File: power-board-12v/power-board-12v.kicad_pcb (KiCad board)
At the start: 2 copper layers, 22.2 x 17.1 mm, 13 parts, among them J1 Conn_01x01, J2 Conn_01x01, J3 Conn_01x04, U1 L78L12_SOT89, U2 L79L12_SOT89, U3 L78L05_SOT89

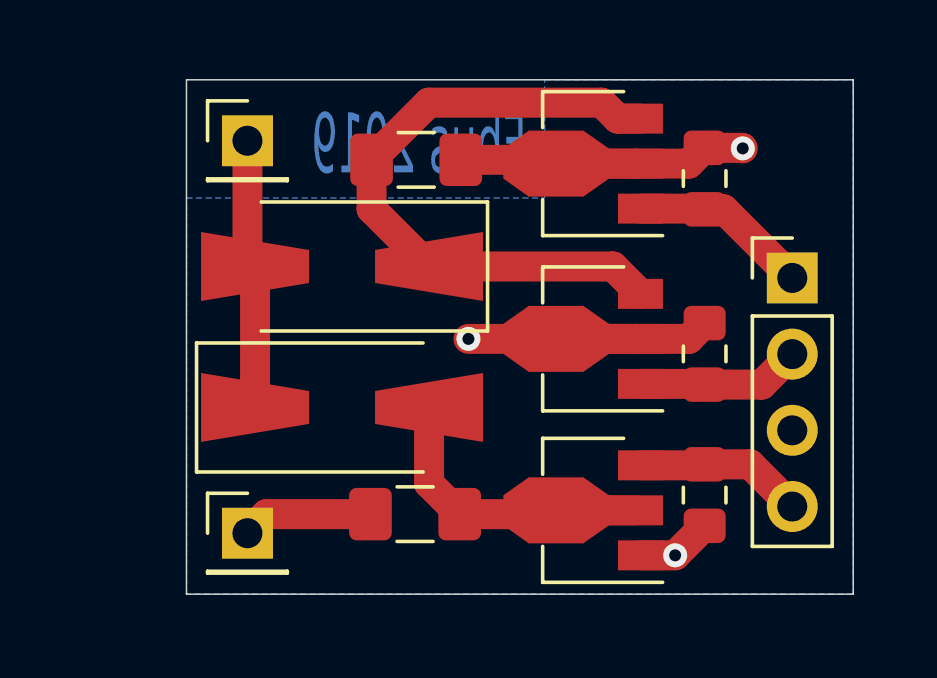
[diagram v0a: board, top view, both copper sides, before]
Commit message: Updated both the amp-and-switch board and the power-board-12v board to version 0.2 after performing bring-up and fixing many issues.
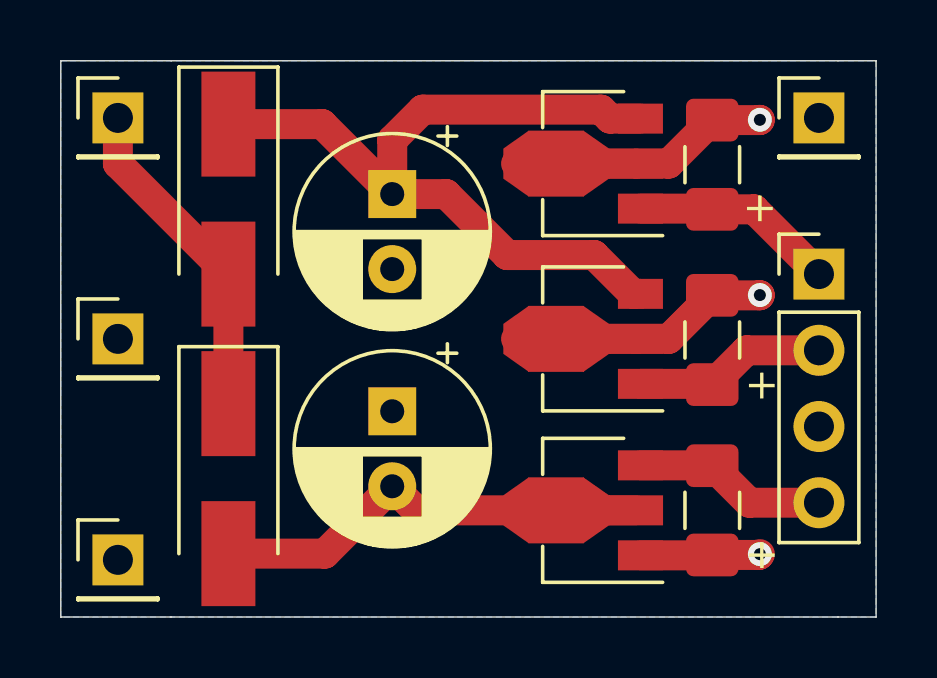
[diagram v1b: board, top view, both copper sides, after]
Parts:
- added J2: Conn_01x01, Connector_PinHeader_2.54mm:PinHeader_1x01_P2.54mm_Vertical, F.Cu at (127.5, 58.2)
- added J2: Conn_01x01, Connector_PinHeader_2.54mm:PinHeader_1x01_P2.54mm_Vertical, F.Cu at (104.1, 72.9)
- C1, C2: value 4.7 uF -> 220 uF; footprint Capacitor_SMD:C_1206_3216Metric_Pad1.42x1.75mm_HandSolder -> Capacitor_THT:CP_Radial_D6.3mm_P2.50mm
- C3, C4, C5: value 0.1 uF -> 4.7 uF; footprint Capacitor_SMD:C_0805_2012Metric_Pad1.15x1.40mm_HandSolder -> Capacitor_SMD:C_1206_3216Metric_Pad1.42x1.75mm_HandSolder
- D1, D2: footprint Diode_SMD:D_SMA-SMB_Universal_Handsoldering -> Diode_SMD:D_SMA_Handsoldering
- moved J2 7.78 mm to (104.1, 65.5)
- moved D2 4.47 mm to (107.8, 70.2), turned to 270 degrees
- moved D1 4.40 mm to (107.8, 60.9), turned to 270 degrees
- moved J1 4.38 mm to (104.1, 58.2)
- moved C2 3.51 mm to (113.3, 67.9), turned to 270 degrees
- moved C1 1.39 mm to (113.3, 60.7), turned to 270 degrees
- moved J3 0.90 mm to (127.5, 63.4)
- moved C4 0.57 mm to (124.0, 71.2)
- moved C3 0.53 mm to (124.0, 65.6)
- moved C5 0.53 mm to (124.0, 59.7)
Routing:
- net Net-(C1-Pad1): track 21.7 -> 26.7 mm
- net Net-(C2-Pad2): track 9.91 -> 14.9 mm
- net GND: track 24.7 -> 21.6 mm
- net Net-(D1-Pad2): track 9.00 -> 11.1 mm
- net Net-(C3-Pad1): track 5.49 -> 6.43 mm
- net Net-(C5-Pad1): track 6.02 -> 6.85 mm
- net Net-(C4-Pad2): track 5.66 -> 6.47 mm
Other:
- board size 22.2 x 17.1 mm -> 27.2 x 18.5 mm
- board text added: "+"
- board text added: "Ole Radio Input Switch Power 12V End Ground Version 0.2"
- board text removed: "Ole Radio Input Switch Power 12V End Ground Version 0.1"
